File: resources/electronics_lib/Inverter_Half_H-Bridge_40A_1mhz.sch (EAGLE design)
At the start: 7 parts

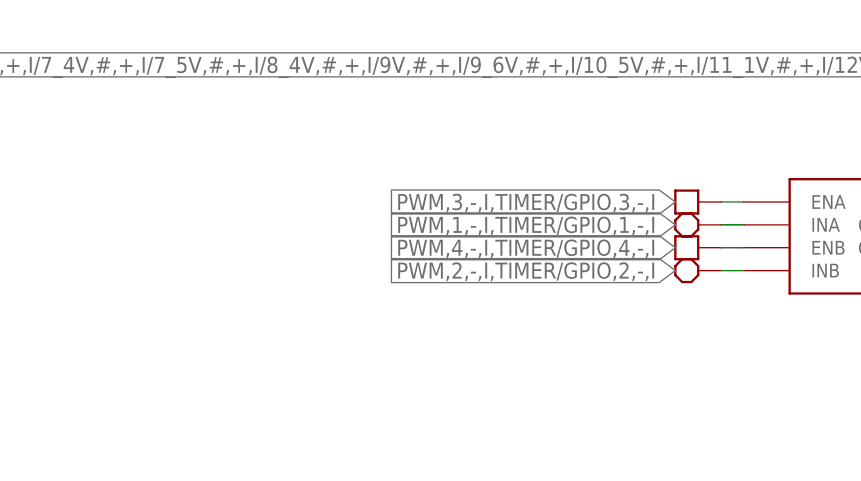
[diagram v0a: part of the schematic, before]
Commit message: Updated Electronics Block Library.
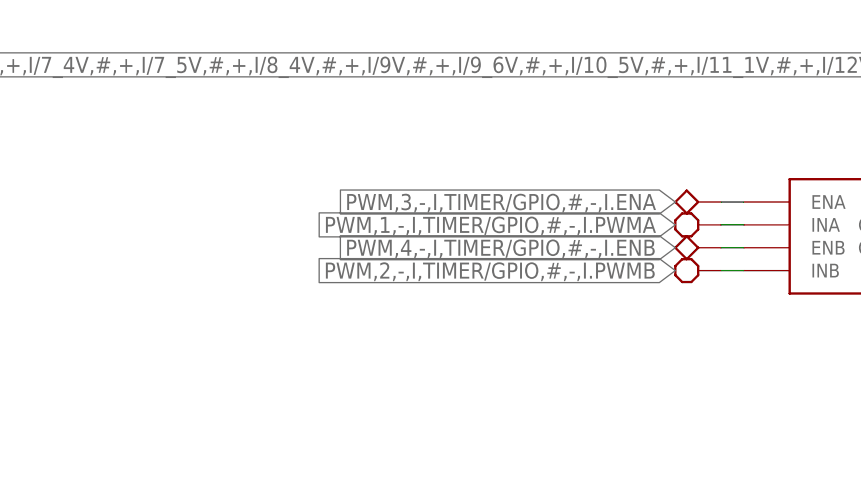
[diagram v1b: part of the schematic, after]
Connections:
- net PWM,1,-,I,TIMER/GPIO,1,-,I renamed PWM,1,-,I,TIMER/GPIO,#,-,I.PWMA
- net PWM,2,-,I,TIMER/GPIO,2,-,I renamed PWM,2,-,I,TIMER/GPIO,#,-,I.PWMB
- net PWM,3,-,I,TIMER/GPIO,3,-,I renamed PWM,3,-,I,TIMER/GPIO,#,-,I.ENA
- net PWM,4,-,I,TIMER/GPIO,4,-,I renamed PWM,4,-,I,TIMER/GPIO,#,-,I.ENB
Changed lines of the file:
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@@
 <part name="U$5" library="block_parts" deviceset="BLOCK_REQUIREMENT" device=""/>
 <part name="U$6" library="block_parts" deviceset="BLOCK_REQUIREMENT" device=""/>
-<part name="U$7" library="block_parts" deviceset="BLOCK_OPTIONAL" device=""/>
-<part name="U$8" library="block_parts" deviceset="BLOCK_OPTIONAL" device=""/>
+<part name="U$7" library="block_parts" deviceset="BLOCK_RECOMMENDED" device=""/>
+<part name="U$8" library="block_parts" deviceset="BLOCK_RECOMMENDED" device=""/>
 <part name="U$9" library="block_parts" deviceset="BLOCK_REQUIREMENT" device=""/>
 </parts>
@@
 </segment>
 </net>
-<net name="PWM,1,-,I,TIMER/GPIO,1,-,I" class="0">
+<net name="PWM,1,-,I,TIMER/GPIO,#,-,I.PWMA" class="0">
 <segment>
 <pinref part="U$3" gate="G$1" pin="INA"/>
@@
 </segment>
 </net>
-<net name="PWM,2,-,I,TIMER/GPIO,2,-,I" class="0">
+<net name="PWM,2,-,I,TIMER/GPIO,#,-,I.PWMB" class="0">
 <segment>
 <pinref part="U$3" gate="G$1" pin="INB"/>
@@
 </segment>
 </net>
-<net name="PWM,4,-,I,TIMER/GPIO,4,-,I" class="0">
+<net name="PWM,4,-,I,TIMER/GPIO,#,-,I.ENB" class="0">
 <segment>
 <pinref part="U$3" gate="G$1" pin="ENB"/>
@@
 </segment>
 </net>
-<net name="PWM,3,-,I,TIMER/GPIO,3,-,I" class="0">
+<net name="PWM,3,-,I,TIMER/GPIO,#,-,I.ENA" class="0">
 <segment>
 <pinref part="U$3" gate="G$1" pin="ENA"/>
